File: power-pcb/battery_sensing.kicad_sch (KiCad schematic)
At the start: 12 parts, among them J4 JST PH, J5 JST PH, U10 DS2484R, U11 RFM-0505S, U9 RFM-0505S

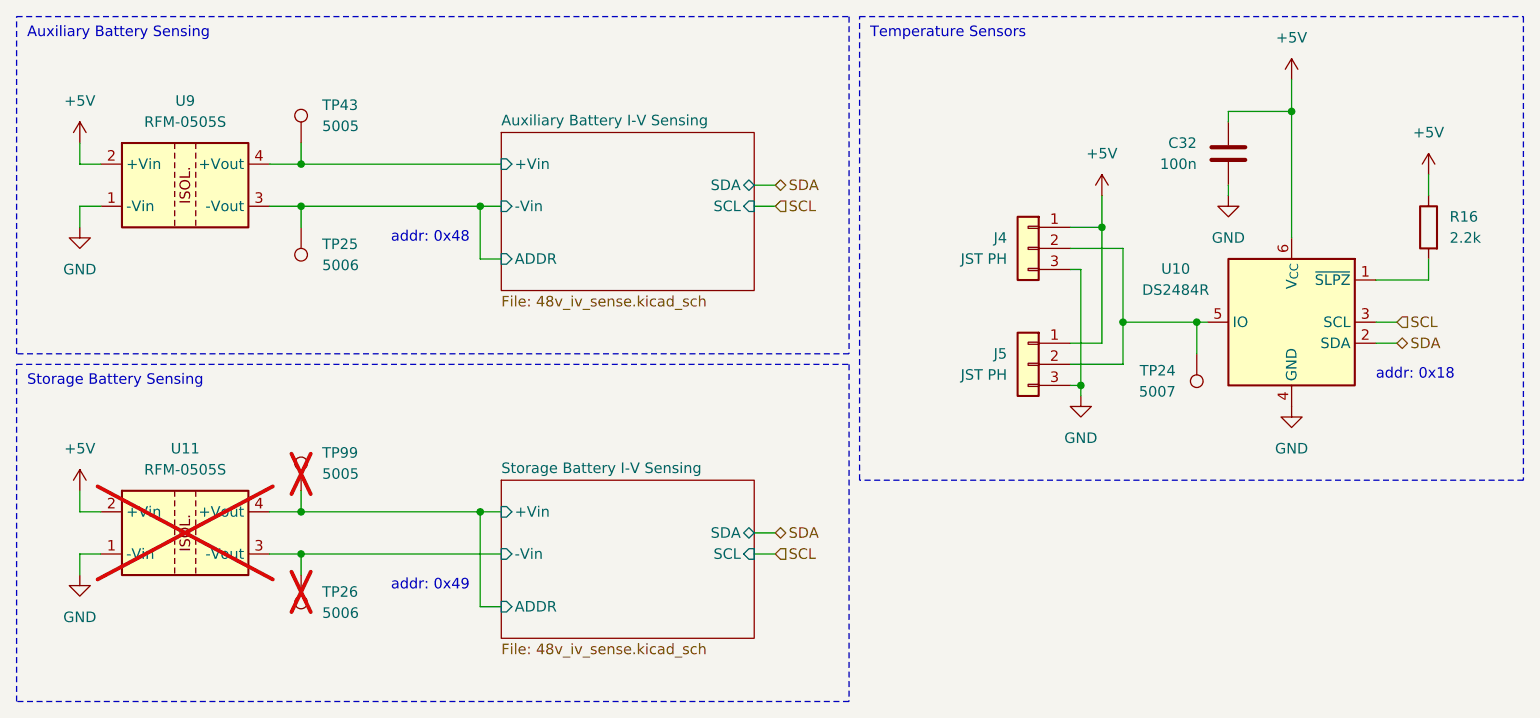
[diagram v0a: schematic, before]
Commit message: power-pcb: finish schematic layout
All parts are placed and connected, ERC passes (except for two
exclusions with comment).
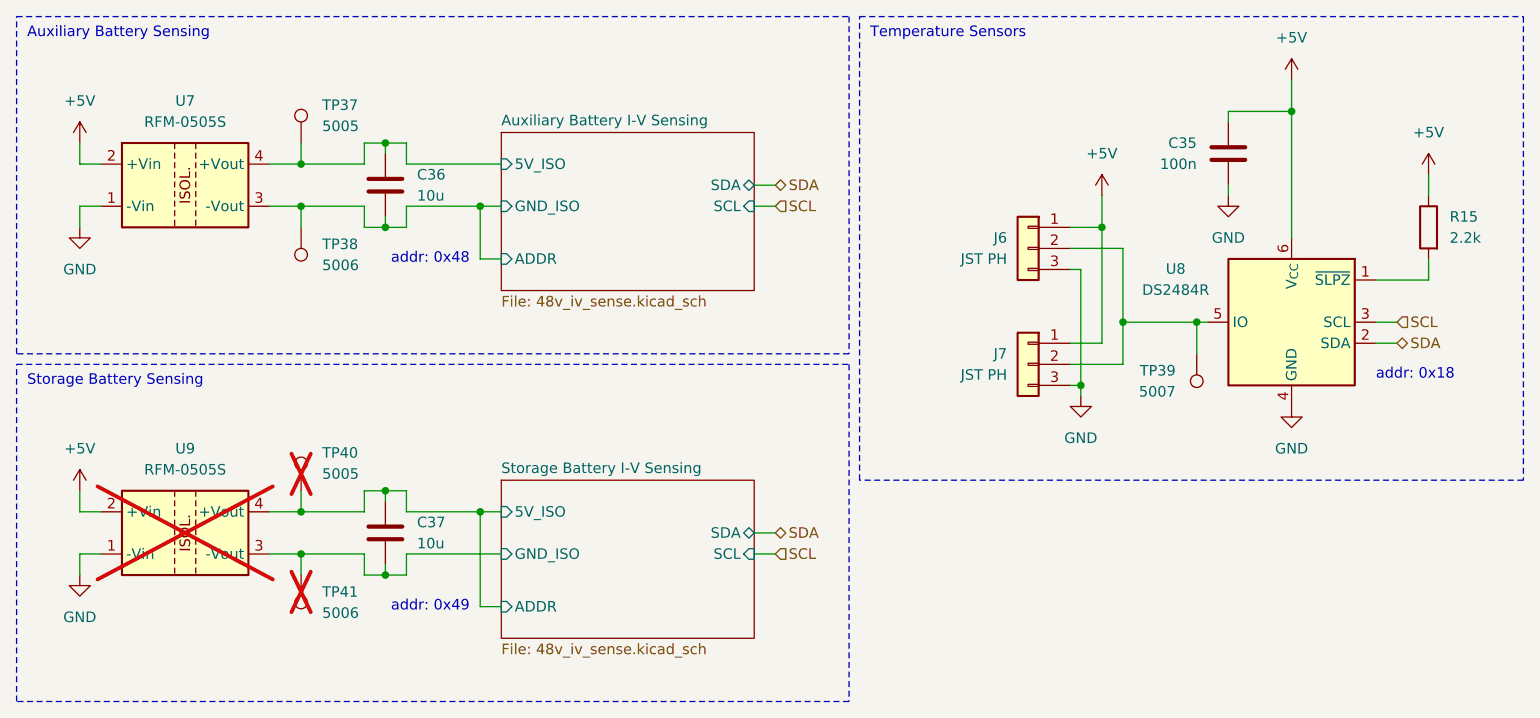
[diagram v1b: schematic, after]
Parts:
- added C36, C37: 10u, Capacitor_SMD:C_1206_3216Metric_Pad1.33x1.80mm_HandSolder, symbol Device:C
- renumbered C32 to C35, J4 to J6, J5 to J7, R16 to R15, TP43 to TP37, TP25 to TP38, TP24 to TP39, TP99 to TP40, TP26 to TP41, U9 to U7, U10 to U8, U11 to U9
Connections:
- net Auxiliary Battery I-V Sensing/+Vin renamed Auxiliary Battery I-V Sensing/5V_ISO
- net Auxiliary Battery I-V Sensing/5V_ISO: now also C36.1
- net Auxiliary Battery I-V Sensing/-Vin renamed Auxiliary Battery I-V Sensing/ADDR
- net Auxiliary Battery I-V Sensing/ADDR: now also C36.2
- net Storage Battery I-V Sensing/+Vin renamed Storage Battery I-V Sensing/5V_ISO
- net Storage Battery I-V Sensing/5V_ISO: now also C37.1
- net Storage Battery I-V Sensing/-Vin renamed Storage Battery I-V Sensing/GND_ISO
- net Storage Battery I-V Sensing/GND_ISO: now also C37.2
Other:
- sheet Auxiliary Battery I-V Sensing ports: added 5V_ISO, GND_ISO; removed +Vin, -Vin
- sheet Storage Battery I-V Sensing ports: added 5V_ISO, GND_ISO; removed +Vin, -Vin
- title: Battery Sensors -> Battery Sensing

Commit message: power-pcb: finish assigning JLCPCB PN
Also assigned missing footprints.
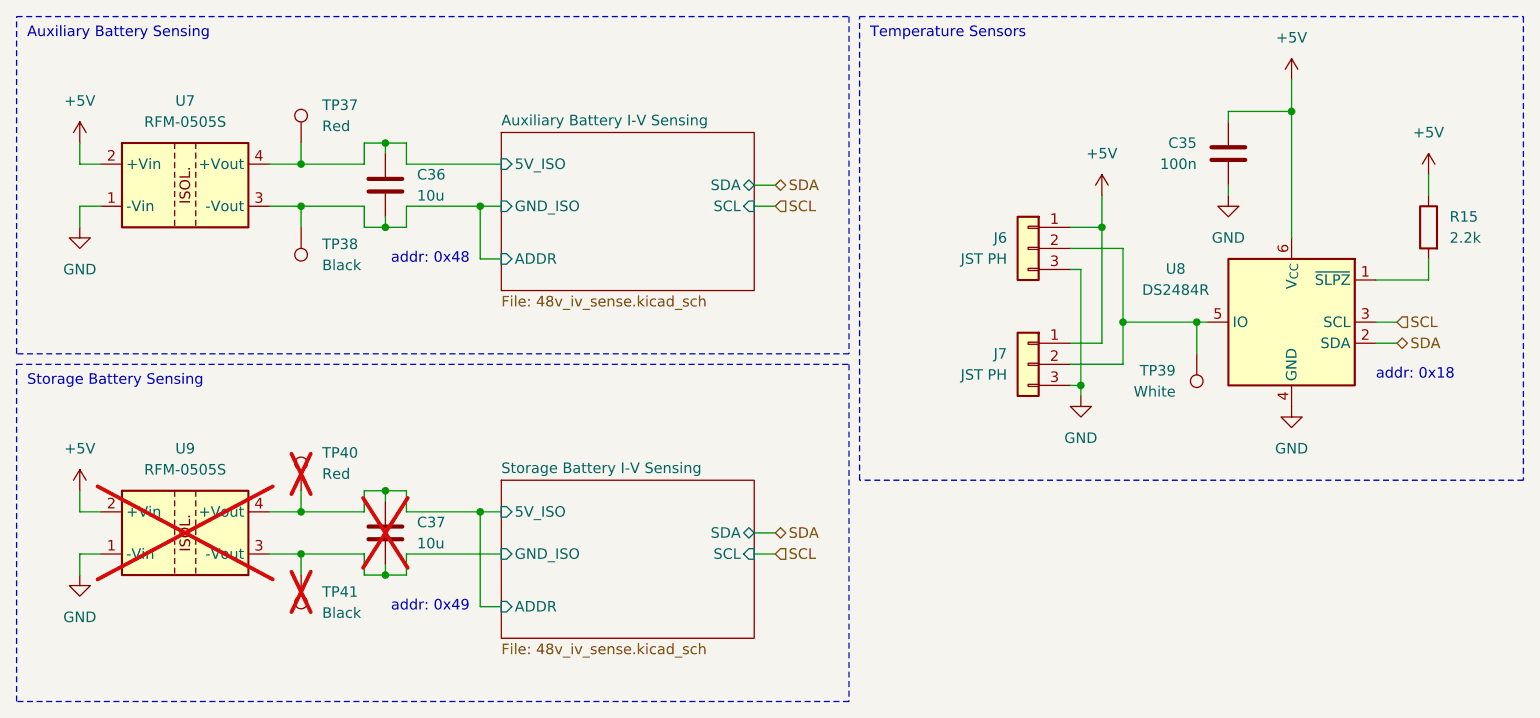
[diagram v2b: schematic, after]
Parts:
- C37: now not fitted
- J6, J7: footprint (none) -> Connector_JST:JST_PH_S3B-PH-K_1x03_P2.00mm_Horizontal; MFR (none) -> JST Sales America Inc.; MPN (none) -> S3B-PH-K-S
- R15: footprint (none) -> Resistor_SMD:R_0603_1608Metric_Pad0.98x0.95mm_HandSolder; JLCPCB (none) -> C4190
- TP37, TP40: value 5005 -> Red; footprint (none) -> TestPoint:TestPoint_Keystone_5005-5009_Compact; MFR (none) -> Keystone Electronics; MPN (none) -> 5005
- TP38, TP41: value 5006 -> Black; footprint (none) -> TestPoint:TestPoint_Keystone_5005-5009_Compact; MFR (none) -> Keystone Electronics; MPN (none) -> 5006
- TP39: value 5007 -> White; footprint (none) -> TestPoint:TestPoint_Keystone_5005-5009_Compact; MFR (none) -> Keystone Electronics; MPN (none) -> 5007
- U7, U9: MFR (none) -> Recom Power; MPN (none) -> RFM-0505S
